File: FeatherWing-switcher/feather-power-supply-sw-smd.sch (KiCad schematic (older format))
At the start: 30 parts, among them J1 5.08mm, J2 Conn_01x12, J3 Conn_01x16, J4 QWIIC, J5 0.1\"x4, Q1 Q_PMOS_GSD, U1 TPS5405DR

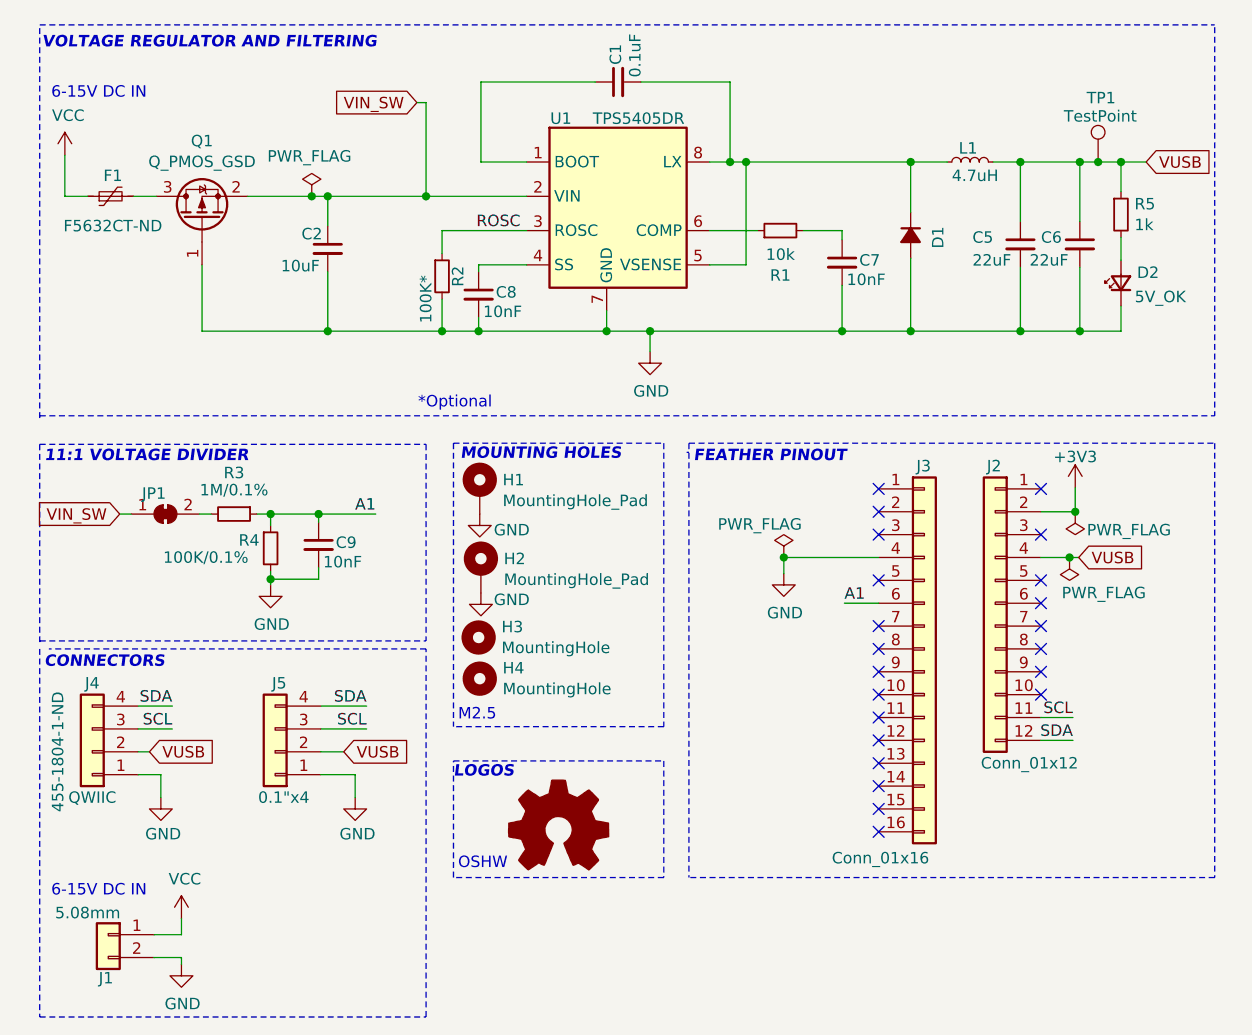
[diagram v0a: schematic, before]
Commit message: minor bom consolidation
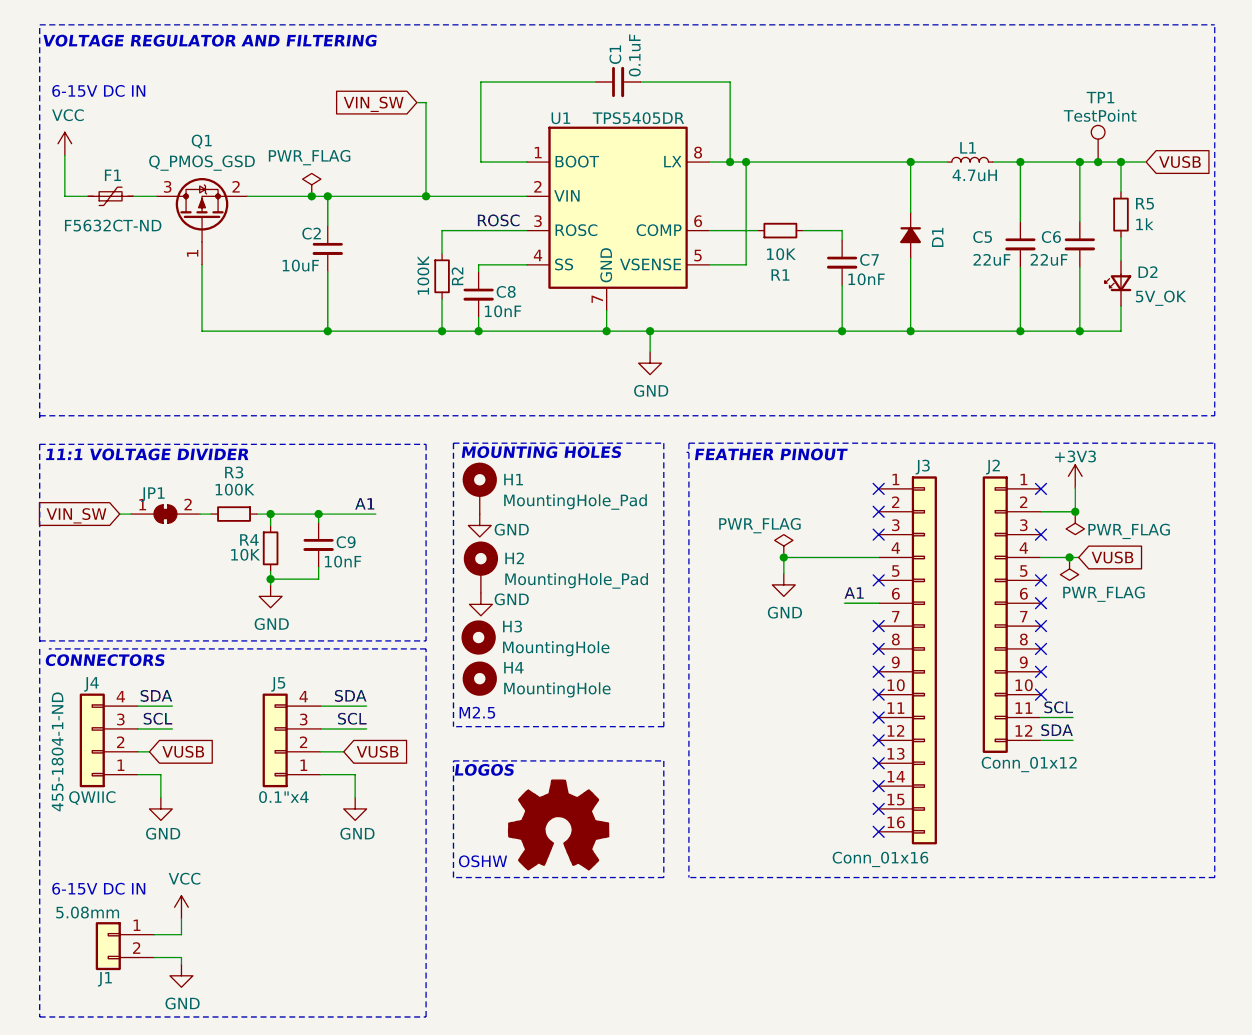
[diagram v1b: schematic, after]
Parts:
- R1: value 10k -> 10K
- R2: value 100K* -> 100K
- R3: value 1M/0.1% -> 100K
- R4: value 100K/0.1% -> 10K
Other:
- note removed: "*Optional"
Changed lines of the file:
@@
 P 6310 2470
 F 0 "R1" V 6114 2470 50  0000 C CNN
-F 1 "10k" V 6205 2470 50  0000 C CNN
+F 1 "10K" V 6205 2470 50  0000 C CNN
 F 2 "Resistor_SMD:R_0603_1608Metric_Pad1.05x0.95mm_HandSolder" H 6310 2470 50  0001 C CNN
 F 3 "~" H 6310 2470 50  0001 C CNN
@@
 P 4830 2670
 F 0 "R2" V 4900 2670 50  0000 C CNN
-F 1 "100K*" V 4760 2570 50  0000 C CNN
+F 1 "100K" V 4750 2670 50  0000 C CNN
 F 2 "Resistor_SMD:R_0603_1608Metric_Pad1.05x0.95mm_HandSolder" H 4830 2670 50  0001 C CNN
 F 3 "~" H 4830 2670 50  0001 C CNN
@@
 Text Notes 3080 1680 0    50   Italic 10
 VOLTAGE REGULATOR AND FILTERING
-Text Notes 4725 3255 0    50   ~ 0
-*Optional
 $Comp
 L power:PWR_FLAG #FLG01
@@
 P 3920 3710
 F 0 "R3" V 3740 3710 50  0000 C CNN
-F 1 "1M/0.1%" V 3815 3710 50  0000 C CNN
+F 1 "100K" V 3815 3710 50  0000 C CNN
 F 2 "Resistor_SMD:R_0603_1608Metric_Pad1.05x0.95mm_HandSolder" H 3920 3710 50  0001 C CNN
 F 3 "~" H 3920 3710 50  0001 C CNN
@@
 P 4080 3860
 F 0 "R4" H 3940 3895 50  0000 L CNN
-F 1 "100K/0.1%" H 3610 3820 50  0000 L CNN
+F 1 "10K" H 3900 3830 50  0000 L CNN
 F 2 "Resistor_SMD:R_0603_1608Metric_Pad1.05x0.95mm_HandSolder" H 4080 3860 50  0001 C CNN
 F 3 "~" H 4080 3860 50  0001 C CNN

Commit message: reduce ground pour clearance
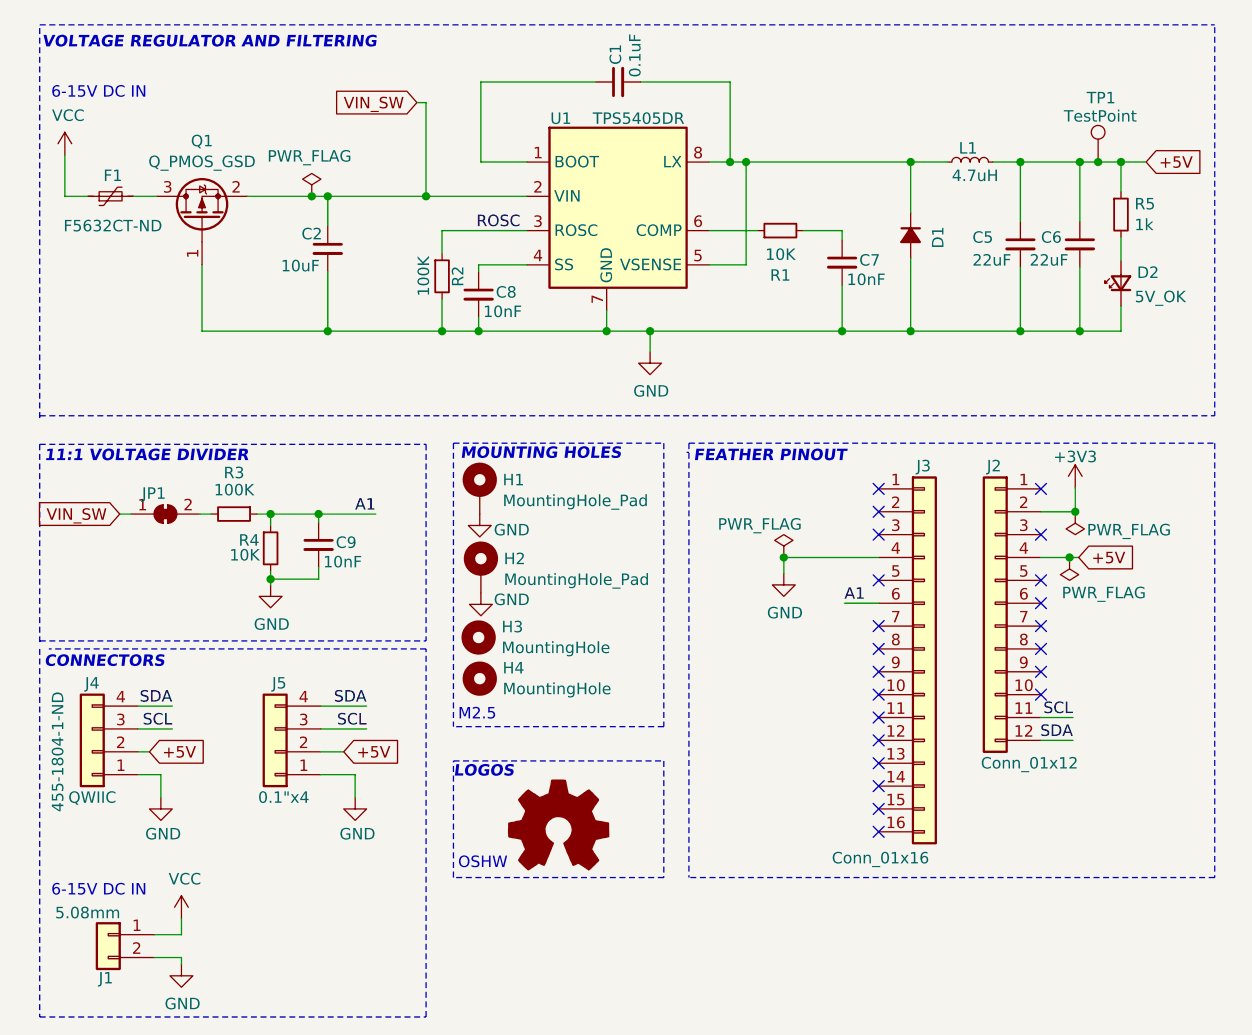
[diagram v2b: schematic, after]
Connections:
- net VUSB renamed +5V
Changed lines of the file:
@@
 $EndComp
 Text GLabel 7615 3900 2    50   Input ~ 0
-VUSB
++5V
 Wire Wire Line
 	7450 3900 7575 3900
@@
 $EndComp
 Text GLabel 7910 2170 2    50   Input ~ 0
-VUSB
++5V
 $Comp
 L Device:C_Small C8
@@
 SCL
 Text GLabel 3550 4750 2    50   Input ~ 0
-VUSB
++5V
 Wire Wire Line
 	3500 4750 3550 4750
@@
 	4300 4650 4500 4650
 Text GLabel 4400 4750 2    50   Input ~ 0
-VUSB
++5V
 $Comp
 L power:GND #PWR08

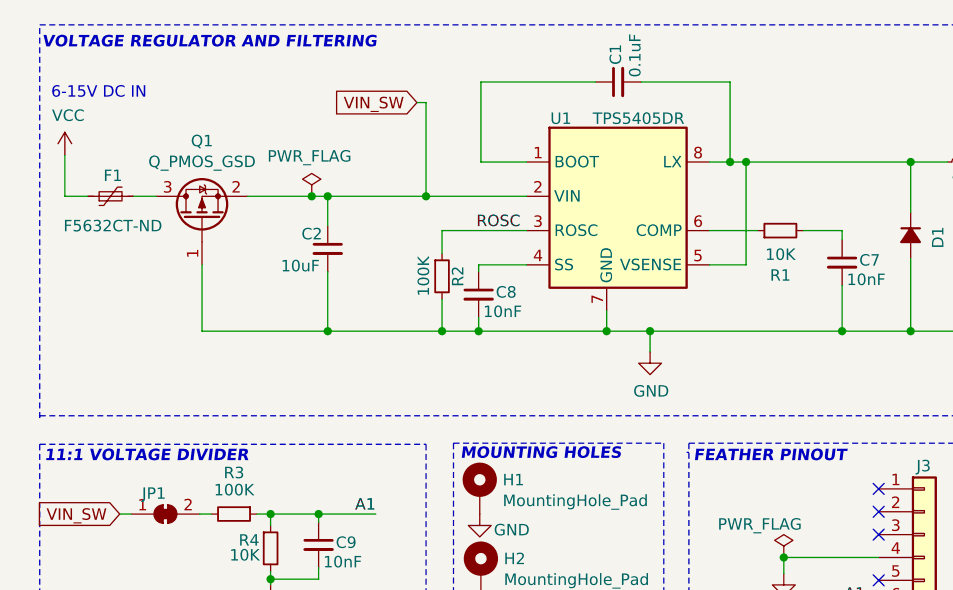
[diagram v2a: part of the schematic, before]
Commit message: updates pad clearance and bom
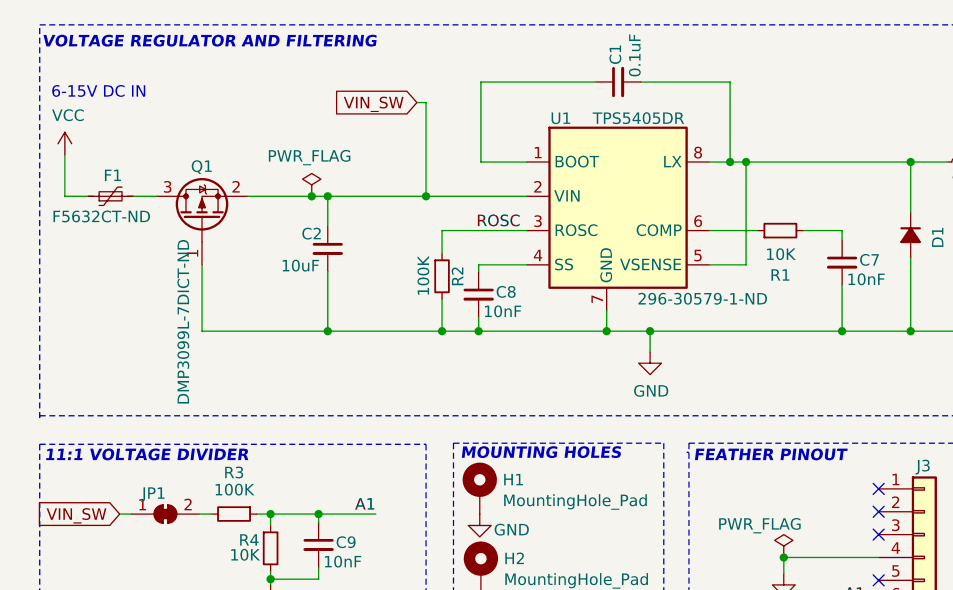
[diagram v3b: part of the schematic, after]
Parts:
- Q1: footprint Package_TO_SOT_SMD:TSOT-23 -> Package_TO_SOT_SMD:SOT-23; Digikey_PN (none) -> DMP3099L-7DICT-ND; MPN (none) -> DMP3099L-7
- U1: Digikey_PN (none) -> 296-30579-1-ND; MPN (none) -> TPS5405DR
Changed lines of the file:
@@
 Sheet 1 1
 Title "Feather Switcher"
-Date "2020-09-01"
+Date "2020-09-21"
 Rev "0.1"
 Comp ""
@@
 F 2 "digikey-footprints:SOIC-8_W3.9mm" H 5650 1870 50  0001 L CIN
 F 3 "https://www.ti.com/lit/ds/symlink/tps5405.pdf" H 5600 2320 50  0001 C CNN
+F 4 "TPS5405DR" H 5600 2320 50  0001 C CNN "MPN"
+F 5 "296-30579-1-ND" H 5970 1870 50  0000 C CNN "Digikey_PN"
 	1    5600 2320
 	1    0    0    -1
@@
 F 2 "Fuse:Fuse_1812_4532Metric_Castellated" H 3430 2120 50  0001 L CNN
 F 3 "~" H 3380 2320 50  0001 C CNN
-F 4 "F5632CT-ND" V 3250 2310 50  0000 C CNN "DigiKey-PN"
+F 4 "F5632CT-ND" V 3290 2360 50  0000 C CNN "DigiKey-PN"
 F 5 "1812L110/24DR" V 3380 2320 50  0001 C CNN "MPN"
 F 6 "Littelfuse Inc." V 3380 2320 50  0001 C CNN "LittleFuse"
@@
 U 1 1 5F6B889D
 P 3780 2420
-F 0 "Q1" V 4122 2420 50  0000 C CNN
-F 1 "Q_PMOS_GSD" V 4031 2420 50  0000 C CNN
-F 2 "Package_TO_SOT_SMD:TSOT-23" H 3980 2520 50  0001 C CNN
-F 3 "~" H 3780 2420 50  0001 C CNN
+F 0 "Q1" V 4010 2420 50  0000 C CNN
+F 1 "Q_PMOS_GSD" V 4031 2420 50  0001 C CNN
+F 2 "Package_TO_SOT_SMD:SOT-23" H 3980 2520 50  0001 C CNN
+F 3 "https://www.diodes.com/assets/Datasheets/DMP3099L.pdf" H 3780 2420 50  0001 C CNN
+F 4 "DMP3099L-7" V 3780 2420 50  0001 C CNN "MPN"
+F 5 "DMP3099L-7DICT-ND" H 3330 2500 50  0000 C CNN "Digikey_PN"
 	1    3780 2420
 	0    -1   -1   0
